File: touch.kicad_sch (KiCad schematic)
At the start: 19 parts, among them J3 Touch_Surface_Top, J4 Touch_Surface_Bottom, U6 CAP1208-1-A4-TR, U7 CAP1208-1-A4-TR

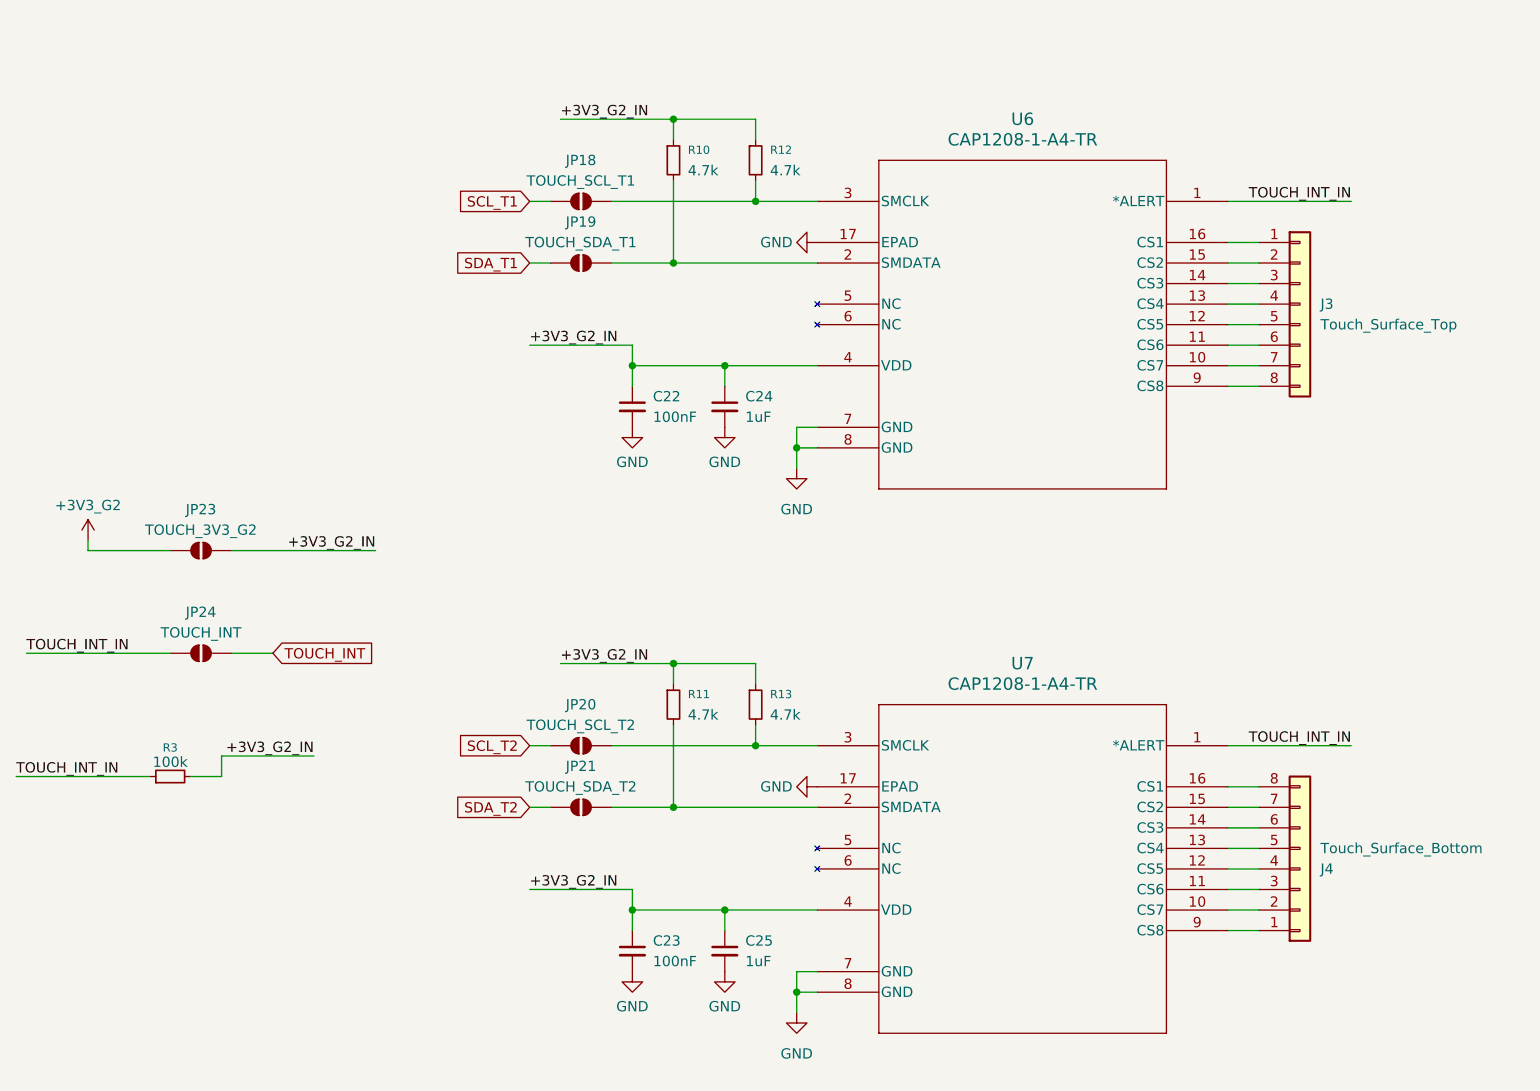
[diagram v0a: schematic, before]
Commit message: remove all jumpers
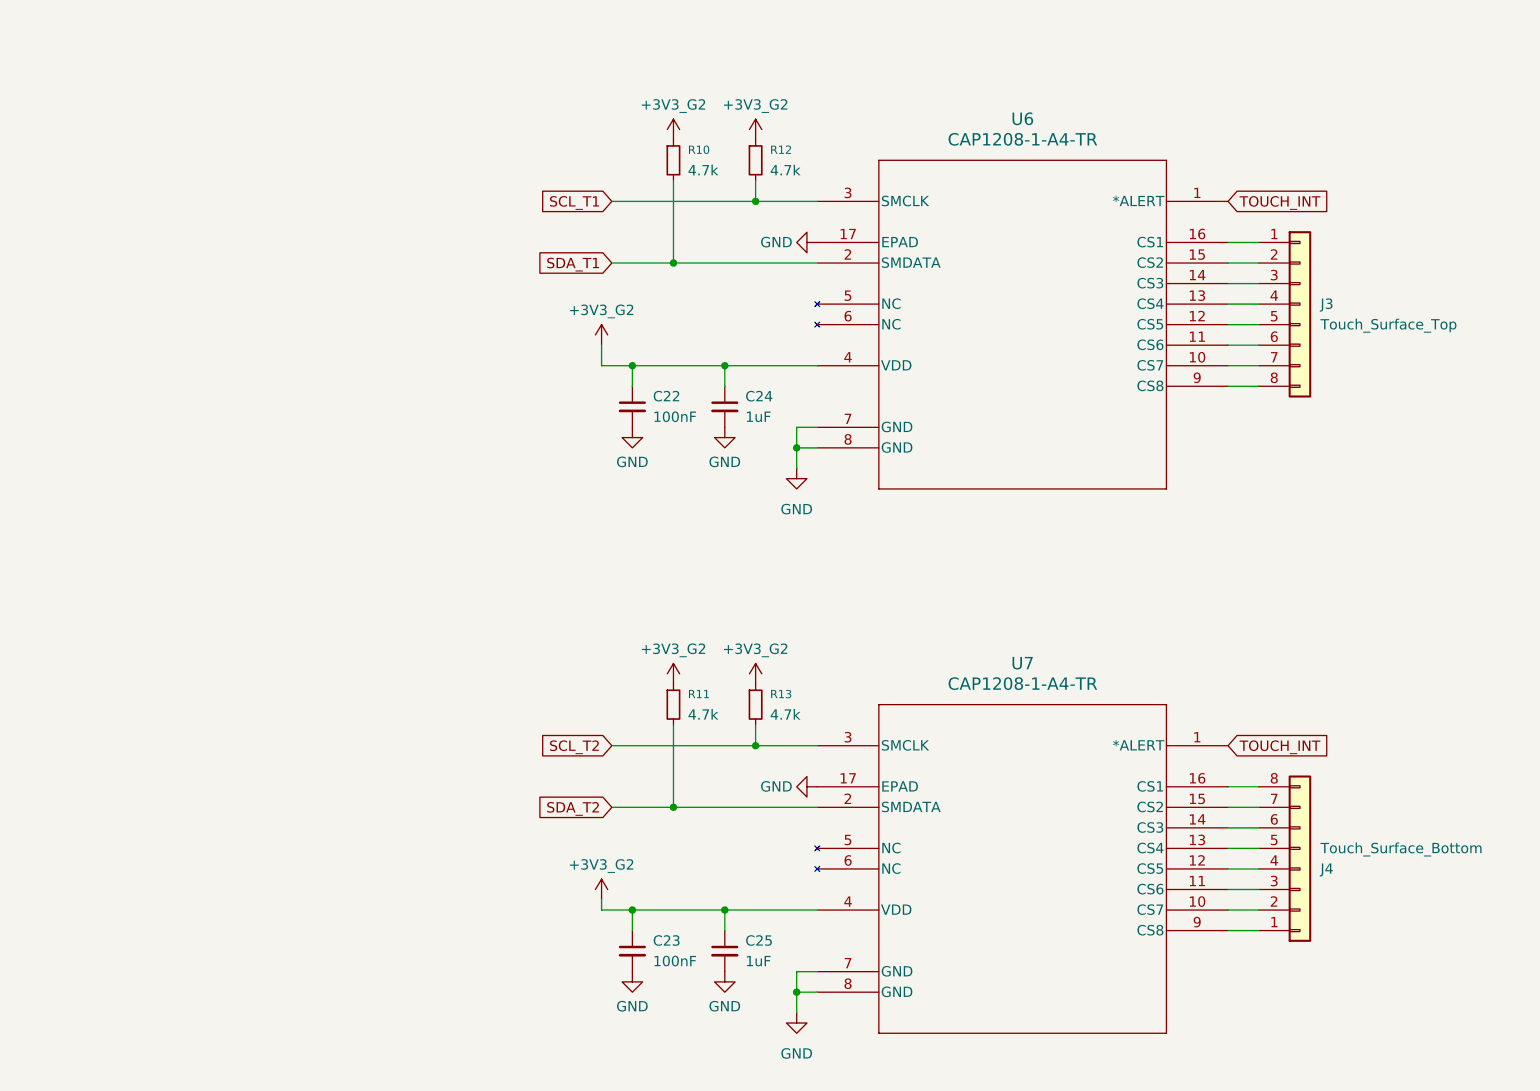
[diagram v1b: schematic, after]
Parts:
- removed JP18: TOUCH_SCL_T1, Jumper:SolderJumper-2_P1.3mm_Open_Pad1.0x1.5mm, symbol Jumper:SolderJumper_2_Open
- removed JP19: TOUCH_SDA_T1, Jumper:SolderJumper-2_P1.3mm_Open_Pad1.0x1.5mm, symbol Jumper:SolderJumper_2_Open
- removed JP20: TOUCH_SCL_T2, Jumper:SolderJumper-2_P1.3mm_Open_Pad1.0x1.5mm, symbol Jumper:SolderJumper_2_Open
- removed JP21: TOUCH_SDA_T2, Jumper:SolderJumper-2_P1.3mm_Open_Pad1.0x1.5mm, symbol Jumper:SolderJumper_2_Open
- removed JP23: TOUCH_3V3_G2, Jumper:SolderJumper-2_P1.3mm_Open_Pad1.0x1.5mm, symbol Jumper:SolderJumper_2_Open
- removed JP24: TOUCH_INT, Jumper:SolderJumper-2_P1.3mm_Open_Pad1.0x1.5mm, symbol Jumper:SolderJumper_2_Open
- removed R3: 100k, Resistor_SMD:R_0402_1005Metric, symbol Device:R_Small
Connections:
- net +3V3_G2_IN is gone; now on net +3V3_G2: C22.1, C23.1, C24.1, C25.1, R10.1, R11.1, R12.1, R13.1, U6.4 (VDD), U7.4 (VDD)
- net TOUCH_INT_IN is gone; now on net TOUCH_INT: U6.1 (*ALERT), U7.1 (*ALERT)
- net SCL_T1: now also R12.2, U6.3 (SMCLK)
- net SCL_T2: now also R13.2, U7.3 (SMCLK)
- net SDA_T1: now also R10.2, U6.2 (SMDATA)
- net SDA_T2: now also R11.2, U7.2 (SMDATA)

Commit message: progress
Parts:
- J3, J4: footprint custom_footprints:Touch_Surface_8_Pad -> custom_footprints:Touch_Surface_8_Pad_Slim
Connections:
- net SCL_T1: now also R13.2, U7.3 (SMCLK); no longer R12.2, U6.3 (SMCLK)
- net SCL_T2: now also R12.2, U6.3 (SMCLK); no longer R13.2, U7.3 (SMCLK)
- net SDA_T1: now also R11.2, U7.2 (SMDATA); no longer R10.2, U6.2 (SMDATA)
- net SDA_T2: now also R10.2, U6.2 (SMDATA); no longer R11.2, U7.2 (SMDATA)
- net at U7.10 (CS7): now also J4.7 (Pin_7); no longer J4.2 (Pin_2)
- net at U7.11 (CS6): now also J4.6 (Pin_6); no longer J4.3 (Pin_3)
- net at U7.12 (CS5): now also J4.5 (Pin_5); no longer J4.4 (Pin_4)
- net at U7.13 (CS4): now also J4.4 (Pin_4); no longer J4.5 (Pin_5)
- net at U7.14 (CS3): now also J4.3 (Pin_3); no longer J4.6 (Pin_6)
- net at U7.15 (CS2): now also J4.2 (Pin_2); no longer J4.7 (Pin_7)
- net at U7.16 (CS1): now also J4.1 (Pin_1); no longer J4.8 (Pin_8)
- net at U7.9 (CS8): now also J4.8 (Pin_8); no longer J4.1 (Pin_1)

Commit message: progress mid-finagling
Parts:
- removed U6, U7: CAP1208-1-A4-TR, QFN16_3x3MC_MCH, symbol CAP1208-1-A4-TR:CAP1208-1-A4-TR
- added R19, R3: 75k, Resistor_SMD:R_0402_1005Metric, symbol Device:R_Small
- added U6, U7: MPR121QR2, Package_DFN_QFN:UQFN-20_3x3mm_P0.4mm, symbol Sensor_Touch:MPR121QR2
- C24, C25: value 1uF -> 100nF
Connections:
- net +3V3_G2: now also U6.20 (VDD), U7.20 (VDD); no longer C22.1, C23.1
- net GND: now also R19.1, R3.1, U6.4 (ADDR), U6.6 (VSS), U7.4 (ADDR), U7.6 (VSS)
- net SCL_T1: now also U7.3 (SDA)
- net SCL_T2: now also U6.3 (SDA)
- net SDA_T1: now also U7.2 (SCL)
- net SDA_T2: now also U6.2 (SCL)
- net TOUCH_INT: now also U6.1 (~{IRQ}), U7.1 (~{IRQ})
- net at J3.1 (Pin_1): now also U6.19 (LED7/ELE11)
- net at J3.2 (Pin_2): now also U6.18 (LED6/ELE10)
- net at J3.3 (Pin_3): now also U6.17 (LED5/ELE9)
- net at J3.4 (Pin_4): now also U6.16 (LED4/ELE8)
- net at J3.5 (Pin_5): now also U6.15 (LED3/ELE7)
- net at J3.6 (Pin_6): now also U6.14 (LED2/ELE6)
- net at J3.7 (Pin_7): now also U6.13 (LED1/ELE5)
- net at J3.8 (Pin_8): now also U6.12 (LED0/ELE4)
- net at J4.7 (Pin_7): now also U7.13 (LED1/ELE5)
- net at J4.6 (Pin_6): now also U7.14 (LED2/ELE6)
- net at J4.5 (Pin_5): now also U7.15 (LED3/ELE7)
- net at J4.4 (Pin_4): now also U7.16 (LED4/ELE8)
- net at J4.3 (Pin_3): now also U7.17 (LED5/ELE9)
- net at J4.2 (Pin_2): now also U7.18 (LED6/ELE10)
- net at J4.1 (Pin_1): now also U7.19 (LED7/ELE11)
- net at J4.8 (Pin_8): now also U7.12 (LED0/ELE4)
- new net: R19.2, U6.7 (REXT)
- new net: C23.1, U7.5 (VREG)
- new net: R3.2, U7.7 (REXT)
- new net: C22.1, U6.5 (VREG)
- no-connect marks 0 -> 8
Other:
- moved on the sheet: C22, C23, C24, C25, J3, J4, R10, R11, R12, R13

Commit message: huge progress
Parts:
- U6, U7: LCSC Part (none) -> C91322
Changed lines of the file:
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@@
+			)
+		)
+		(property "LCSC Part" "C91322"
+			(at 166.37 135.89 0)
+			(effects
+				(font
+					(size 1.27 1.27)
+				)
+				(hide yes)
 			)
 		)
@@
 			(at 166.37 68.58 0)
 			(effects
+				(font
+					(size 1.27 1.27)
+				)
+				(hide yes)
+			)
+		)
+		(property "LCSC Part" "C91322"
+			(at 166.37 68.58 0)
+			(effects

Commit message: final fixups before prod
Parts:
- C22: renamed from C25; LCSC Part C52923 -> C1525
- C23: renamed from C24; LCSC Part C52923 -> C1525
- R10: renamed from R3; LCSC Part (none) -> C25798
- R11: renamed from R19; LCSC Part (none) -> C25798
- renumbered C22 to C20, C23 to C21, J3 to J2, J4 to J3, R10 to R8, R11 to R9
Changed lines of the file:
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@@
 		(on_board yes)
 		(dnp no)
-		(property "Reference" "J3"
+		(property "Reference" "J2"
 			(at 190.5 73.6601 0)
 			(effects
@@
 			(project ""
 				(path "/c6cb5a1d-9f97-4766-8582-a9e93ed049e4/7b6f6d0f-0137-41ad-b85b-11085abf19c4"
-					(reference "J3")
+					(reference "J2")
 					(unit 1)
 				)
@@
 		(dnp no)
 		(fields_autoplaced yes)
-		(property "Reference" "#PWR073"
+		(property "Reference" "#PWR058"
 			(at 166.37 41.91 0)
 			(effects
@@
 			(project ""
 				(path "/c6cb5a1d-9f97-4766-8582-a9e93ed049e4/7b6f6d0f-0137-41ad-b85b-11085abf19c4"
-					(reference "#PWR073")
+					(reference "#PWR058")
 					(unit 1)
 				)
@@
 		(on_board yes)
 		(dnp no)
-		(property "Reference" "C24"
+		(property "Reference" "C23"
 			(at 173.99 41.9162 0)
 			(effects
@@
 			)
 		)
-		(property "LCSC Part" "C52923"
+		(property "LCSC Part" "C1525"
 			(at 171.45 43.18 0)
 			(effects
@@
 			(project ""
 				(path "/c6cb5a1d-9f97-4766-8582-a9e93ed049e4/7b6f6d0f-0137-41ad-b85b-11085abf19c4"
-					(reference "C24")
+					(reference "C23")
 					(unit 1)
 				)
@@
 		(dnp no)
 		(fields_autoplaced yes)
-		(property "Reference" "#PWR086"
+		(property "Reference" "#PWR053"
 			(at 146.05 92.71 0)
 			(effects
@@
 			(project ""
 				(path "/c6cb5a1d-9f97-4766-8582-a9e93ed049e4/7b6f6d0f-0137-41ad-b85b-11085abf19c4"
-					(reference "#PWR086")
+					(reference "#PWR053")
 					(unit 1)
 				)
@@
 		(on_board yes)
 		(dnp no)
-		(property "Reference" "#PWR089"
+		(property "Reference" "#PWR052"
 			(at 146.05 52.07 0)
 			(effects
@@
 			(project "rc_keychain"
 				(path "/c6cb5a1d-9f97-4766-8582-a9e93ed049e4/7b6f6d0f-0137-41ad-b85b-11085abf19c4"
-					(reference "#PWR089")
+					(reference "#PWR052")
 					(unit 1)
 				)
@@
 		(on_board yes)
 		(dnp no)
-		(property "Reference" "#PWR067"
+		(property "Reference" "#PWR048"
 			(at 135.89 52.07 0)
 			(effects
@@
 			(project "rc_keychain"
 				(path "/c6cb5a1d-9f97-4766-8582-a9e93ed049e4/7b6f6d0f-0137-41ad-b85b-11085abf19c4"
-					(reference "#PWR067")
+					(reference "#PWR048")
 					(unit 1)
 				)
@@
 		(on_board yes)
 		(dnp no)
-		(property "Reference" "#PWR056"
+		(property "Reference" "#PWR049"
 			(at 135.89 119.38 0)
 			(effects
@@
 			(project ""
 				(path "/c6cb5a1d-9f97-4766-8582-a9e93ed049e4/7b6f6d0f-0137-41ad-b85b-11085abf19c4"
-					(reference "#PWR056")
+					(reference "#PWR049")
 					(unit 1)
 				)
@@
 		(on_board yes)
 		(dnp no)
-		(property "Reference" "#PWR055"
+		(property "Reference" "#PWR057"
 			(at 147.32 135.89 0)
 			(effects
@@
 			(project ""
 				(path "/c6cb5a1d-9f97-4766-8582-a9e93ed049e4/7b6f6d0f-0137-41ad-b85b-11085abf19c4"
-					(reference "#PWR055")
+					(reference "#PWR057")
 					(unit 1)
 				)
@@
 		(dnp no)
 		(fields_autoplaced yes)
-		(property "Reference" "#PWR063"
+		(property "Reference" "#PWR061"
 			(at 166.37 162.56 0)
 			(effects
@@
 			(project ""
 				(path "/c6cb5a1d-9f97-4766-8582-a9e93ed049e4/7b6f6d0f-0137-41ad-b85b-11085abf19c4"
-					(reference "#PWR063")
+					(reference "#PWR061")
 					(unit 1)
 				)
@@
 		(on_board yes)
 		(dnp no)
-		(property "Reference" "#PWR065"
+		(property "Reference" "#PWR055"
 			(at 146.05 160.02 0)
 			(effects
@@
 			(project ""
 				(path "/c6cb5a1d-9f97-4766-8582-a9e93ed049e4/7b6f6d0f-0137-41ad-b85b-11085abf19c4"
-					(reference "#PWR065")
+					(reference "#PWR055")
 					(unit 1)
 				)
@@
 		(dnp no)
 		(fields_autoplaced yes)
-		(property "Reference" "#PWR092"
+		(property "Reference" "#PWR051"
 			(at 137.16 82.55 0)
 			(effects
@@
 			(project "rc_keychain"
 				(path "/c6cb5a1d-9f97-4766-8582-a9e93ed049e4/7b6f6d0f-0137-41ad-b85b-11085abf19c4"
-					(reference "#PWR092")
+					(reference "#PWR051")
 					(unit 1)
 				)
@@
 		(on_board yes)
 		(dnp no)
-		(property "Reference" "R10"
+		(property "Reference" "R8"
 			(at 137.668 49.53 0)
 			(effects
@@
 			(project ""
 				(path "/c6cb5a1d-9f97-4766-8582-a9e93ed049e4/7b6f6d0f-0137-41ad-b85b-11085abf19c4"
-					(reference "R10")
+					(reference "R8")
 					(unit 1)
 				)
@@
 		(dnp no)
 		(fields_autoplaced yes)
-		(property "Reference" "R19"
+		(property "Reference" "R11"
 			(at 142.24 68.58 90)
 			(effects
@@
 			)
 		)
+		(property "LCSC Part" "C25798"
+			(at 142.24 73.66 90)
+			(effects
+				(font
+					(size 1.27 1.27)
+				)
+				(hide yes)
+			)
+		)
 		(pin "2"
 		)
@@
 			(project "rc_keychain"
 				(path "/c6cb5a1d-9f97-4766-8582-a9e93ed049e4/7b6f6d0f-0137-41ad-b85b-11085abf19c4"
-					(reference "R19")
+					(reference "R11")
 					(unit 1)
 				)
@@
 		(dnp no)
 		(fields_autoplaced yes)
-		(property "Reference" "C25"
+		(property "Reference" "C22"
 			(at 172.72 107.9562 0)
 			(effects
@@
 			)
 		)
-		(property "LCSC Part" "C52923"
+		(property "LCSC Part" "C1525"
 			(at 170.18 109.22 0)
 			(effects
@@
 			(project "rc_keychain"
 				(path "/c6cb5a1d-9f97-4766-8582-a9e93ed049e4/7b6f6d0f-0137-41ad-b85b-11085abf19c4"
-					(reference "C25")
+					(reference "C22")
 					(unit 1)
 				)
@@
 		(dnp no)
 		(fields_autoplaced yes)
-		(property "Reference" "C23"
+		(property "Reference" "C21"
 			(at 148.59 149.8662 0)
 			(effects
@@
 			(project "rc_keychain"
 				(path "/c6cb5a1d-9f97-4766-8582-a9e93ed049e4/7b6f6d0f-0137-41ad-b85b-11085abf19c4"
-					(reference "C23")
+					(reference "C21")
 					(unit 1)
 				)
@@
 		(on_board yes)
 		(dnp no)
-		(property "Reference" "#PWR053"
+		(property "Reference" "#PWR056"
 			(at 147.32 68.58 0)
 			(effects
@@
 			(project ""
 				(path "/c6cb5a1d-9f97-4766-8582-a9e93ed049e4/7b6f6d0f-0137-41ad-b85b-11085abf19c4"
-					(reference "#PWR053")
+					(reference "#PWR056")
 					(unit 1)
 				)
@@
 		(on_board yes)
 		(dnp no)
-		(property "Reference" "R11"
+		(property "Reference" "R9"
 			(at 137.668 116.84 0)
 			(effects
@@
 			(project "rc_keychain"
 				(path "/c6cb5a1d-9f97-4766-8582-a9e93ed049e4/7b6f6d0f-0137-41ad-b85b-11085abf19c4"
-					(reference "R11")
+					(reference "R9")
 					(unit 1)
 				)
@@
 		(dnp no)
 		(fields_autoplaced yes)
-		(property "Reference" "C22"
+		(property "Reference" "C20"
 			(at 148.59 82.5562 0)
 			(effects
@@
 			(project ""
 				(path "/c6cb5a1d-9f97-4766-8582-a9e93ed049e4/7b6f6d0f-0137-41ad-b85b-11085abf19c4"
-					(reference "C22")
+					(reference "C20")
 					(unit 1)
 				)
@@
 		(on_board yes)
 		(dnp no)
-		(property "Reference" "#PWR088"
+		(property "Reference" "#PWR063"
 			(at 171.45 52.07 0)
 			(effects
@@
 			(project ""
 				(path "/c6cb5a1d-9f97-4766-8582-a9e93ed049e4/7b6f6d0f-0137-41ad-b85b-11085abf19c4"
-					(reference "#PWR088")
+					(reference "#PWR063")
 					(unit 1)
 				)
@@
 		(dnp no)
 		(fields_autoplaced yes)
-		(property "Reference" "#PWR064"
+		(property "Reference" "#PWR059"
 			(at 166.37 95.25 0)
 			(effects
@@
 			(project ""
 				(path "/c6cb5a1d-9f97-4766-8582-a9e93ed049e4/7b6f6d0f-0137-41ad-b85b-11085abf19c4"
-					(reference "#PWR064")
+					(reference "#PWR059")
 					(unit 1)
 				)
@@
 		(dnp no)
 		(fields_autoplaced yes)
-		(property "Reference" "R3"
+		(property "Reference" "R10"
 			(at 140.97 135.89 90)
 			(effects
@@
 			)
 		)
+		(property "LCSC Part" "C25798"
+			(at 140.97 140.97 90)
+			(effects
+				(font
+					(size 1.27 1.27)
+				)
+				(hide yes)
+			)
+		)
 		(pin "2"
 		)
@@
 			(project ""
 				(path "/c6cb5a1d-9f97-4766-8582-a9e93ed049e4/7b6f6d0f-0137-41ad-b85b-11085abf19c4"
-					(reference "R3")
+					(reference "R10")
 					(unit 1)
 				)
@@
 		(dnp no)
 		(fields_autoplaced yes)
-		(property "Reference" "#PWR091"
+		(property "Reference" "#PWR050"
 			(at 135.89 149.86 0)
 			(effects
@@
 			(project ""
 				(path "/c6cb5a1d-9f97-4766-8582-a9e93ed049e4/7b6f6d0f-0137-41ad-b85b-11085abf19c4"
-					(reference "#PWR091")
+					(reference "#PWR050")
 					(unit 1)
 				)
@@
 		(on_board yes)
 		(dnp no)
-		(property "Reference" "#PWR0125"
+		(property "Reference" "#PWR060"
 			(at 166.37 107.95 0)
 			(effects
@@
 			(project "rc_keychain"
 				(path "/c6cb5a1d-9f97-4766-8582-a9e93ed049e4/7b6f6d0f-0137-41ad-b85b-11085abf19c4"
-					(reference "#PWR0125")
+					(reference "#PWR060")
 					(unit 1)
 				)
@@
 		(on_board yes)
 		(dnp no)
-		(property "Reference" "J4"
+		(property "Reference" "J3"
 			(at 190.5 140.9701 0)
 			(effects
@@
 			(project "rc_keychain"
 				(path "/c6cb5a1d-9f97-4766-8582-a9e93ed049e4/7b6f6d0f-0137-41ad-b85b-11085abf19c4"
-					(reference "J4")
+					(reference "J3")
 					(unit 1)
 				)
@@
 		(on_board yes)
 		(dnp no)
-		(property "Reference" "#PWR066"
+		(property "Reference" "#PWR054"
 			(at 146.05 119.38 0)
 			(effects
@@
 			(project "rc_keychain"
 				(path "/c6cb5a1d-9f97-4766-8582-a9e93ed049e4/7b6f6d0f-0137-41ad-b85b-11085abf19c4"
-					(reference "#PWR066")
+					(reference "#PWR054")
 					(unit 1)
 				)
@@
 		(on_board yes)
 		(dnp no)
-		(property "Reference" "#PWR059"
+		(property "Reference" "#PWR062"
 			(at 170.18 118.11 0)
 			(effects
@@
 			(project "rc_keychain"
 				(path "/c6cb5a1d-9f97-4766-8582-a9e93ed049e4/7b6f6d0f-0137-41ad-b85b-11085abf19c4"
-					(reference "#PWR059")
-					(unit 1)
-				)
+					(reference "#PWR062")
+					(unit 1)
+				)
